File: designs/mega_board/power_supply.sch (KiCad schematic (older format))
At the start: 11 parts

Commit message: Add BOM definition to all resistors
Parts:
- R18, R60: Manufacturer (none) -> Panasonic Electronic Components; Manufacturer PN (none) -> ERJ-PA2F1003X; Supplier (none) -> DigiKey; Supplier PN (none) -> P17236DKR-ND
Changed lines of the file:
@@
 F 2 "LibreRouter_MegaBoard:R0402" V 2530 3650 50  0001 C CNN
 F 3 "~" H 2600 3650 50  0001 C CNN
+F 4 "Panasonic Electronic Components" H 2600 3650 50  0001 C CNN "Manufacturer"
+F 5 "ERJ-PA2F1003X" H 2600 3650 50  0001 C CNN "Manufacturer PN"
+F 6 "DigiKey" H 2600 3650 50  0001 C CNN "Supplier"
+F 7 "P17236DKR-ND" H 2600 3650 50  0001 C CNN "Supplier PN"
 	1    2600 3650
 	1    0    0    -1
@@
 F 2 "LibreRouter_MegaBoard:R0402" V 7480 3650 50  0001 C CNN
 F 3 "~" H 7550 3650 50  0001 C CNN
+F 4 "Panasonic Electronic Components" H 7550 3650 50  0001 C CNN "Manufacturer"
+F 5 "ERJ-PA2F1003X" H 7550 3650 50  0001 C CNN "Manufacturer PN"
+F 6 "DigiKey" H 7550 3650 50  0001 C CNN "Supplier"
+F 7 "P17236DKR-ND" H 7550 3650 50  0001 C CNN "Supplier PN"
 	1    7550 3650
 	1    0    0    -1

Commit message: Add some more BOM components definition
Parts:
- L1: Manufacturer (none) -> Littelfuse Inc.; Manufacturer PN (none) -> RUEF400-2; Supplier (none) -> DigiKey; Supplier PN (none) -> RUEF400-2HFCT-ND
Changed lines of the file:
@@
 F 2 "LibreRouter_MegaBoard:GR72-135" H 4150 900 50  0001 L CNN
 F 3 "~" H 4100 1100 50  0001 C CNN
+F 4 "Littelfuse Inc." H 4100 1100 50  0001 C CNN "Manufacturer"
+F 5 "RUEF400-2" H 4100 1100 50  0001 C CNN "Manufacturer PN"
+F 6 "DigiKey" H 4100 1100 50  0001 C CNN "Supplier"
+F 7 "RUEF400-2HFCT-ND" H 4100 1100 50  0001 C CNN "Supplier PN"
 	1    4100 1100
 	0    1    1    0

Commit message: Add some missing BOM details for components that are not in common suppliers
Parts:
- V1: Manufacturer (none) -> Bincheng Electronics; Manufacturer PN (none) -> BC301N-D
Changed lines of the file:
@@
 F 2 "LibreRouter_MegaBoard:BC301N-D" H 2900 1450 50  0001 C CNN
 F 3 "" H 2900 1450 50  0001 C CNN
+F 4 "Bincheng Electronics" H 2900 1450 50  0001 C CNN "Manufacturer"
+F 5 "BC301N-D" H 2900 1450 50  0001 C CNN "Manufacturer PN"
 	1    2900 1450
 	1    0    0    -1

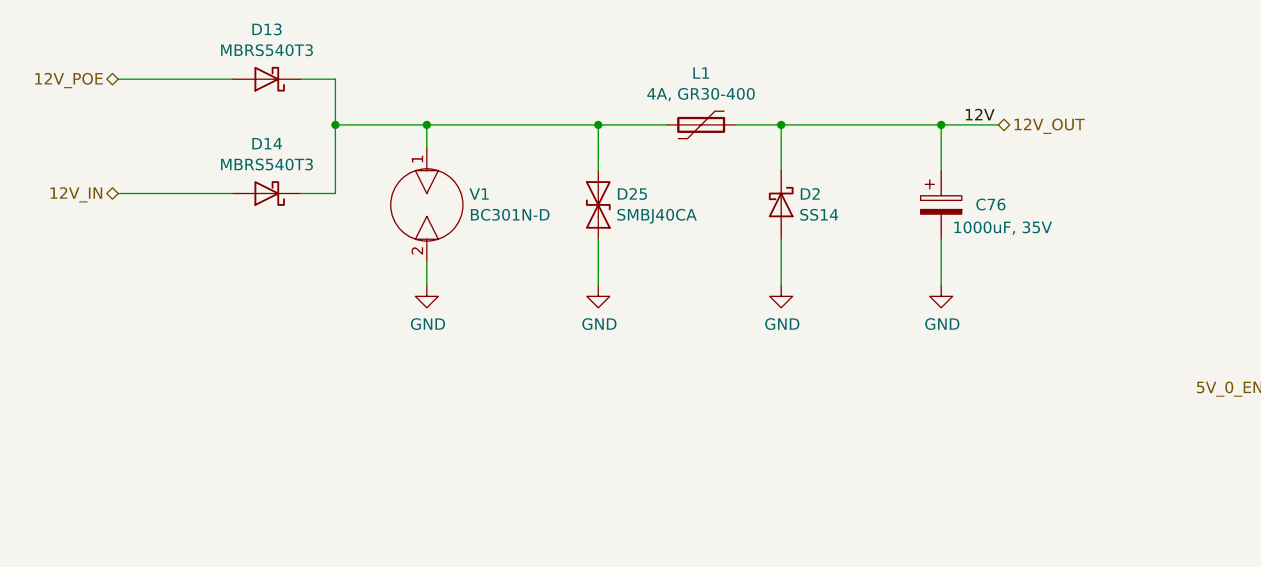
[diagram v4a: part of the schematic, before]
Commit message: Add poe input output dual circuit
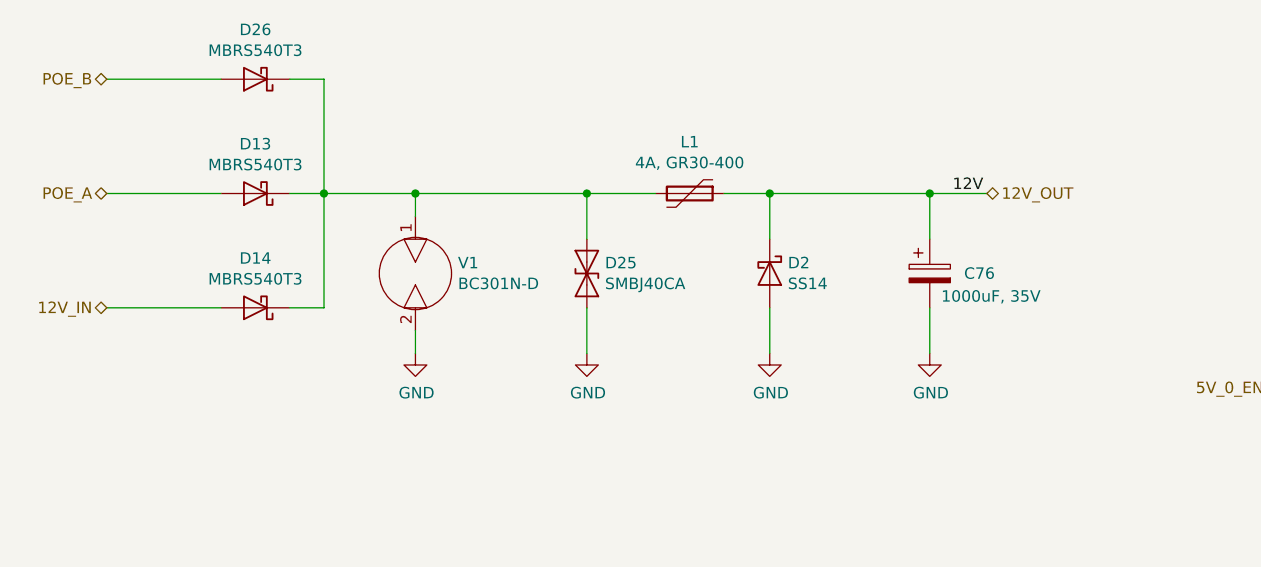
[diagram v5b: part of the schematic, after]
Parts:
- added D26: MBRS540T3, LibreRouter_MegaBoard:SMC, symbol Device:D_Schottky
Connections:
- net at D13.1 (K), D14.1 (K), D25.1 (A1)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: now also D26.1 (K)
- net 12V_POE renamed POE_A
- new net POE_B: D26.2 (A)
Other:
- moved on the sheet: C76, D13, D14, D2, D25, L1, V1

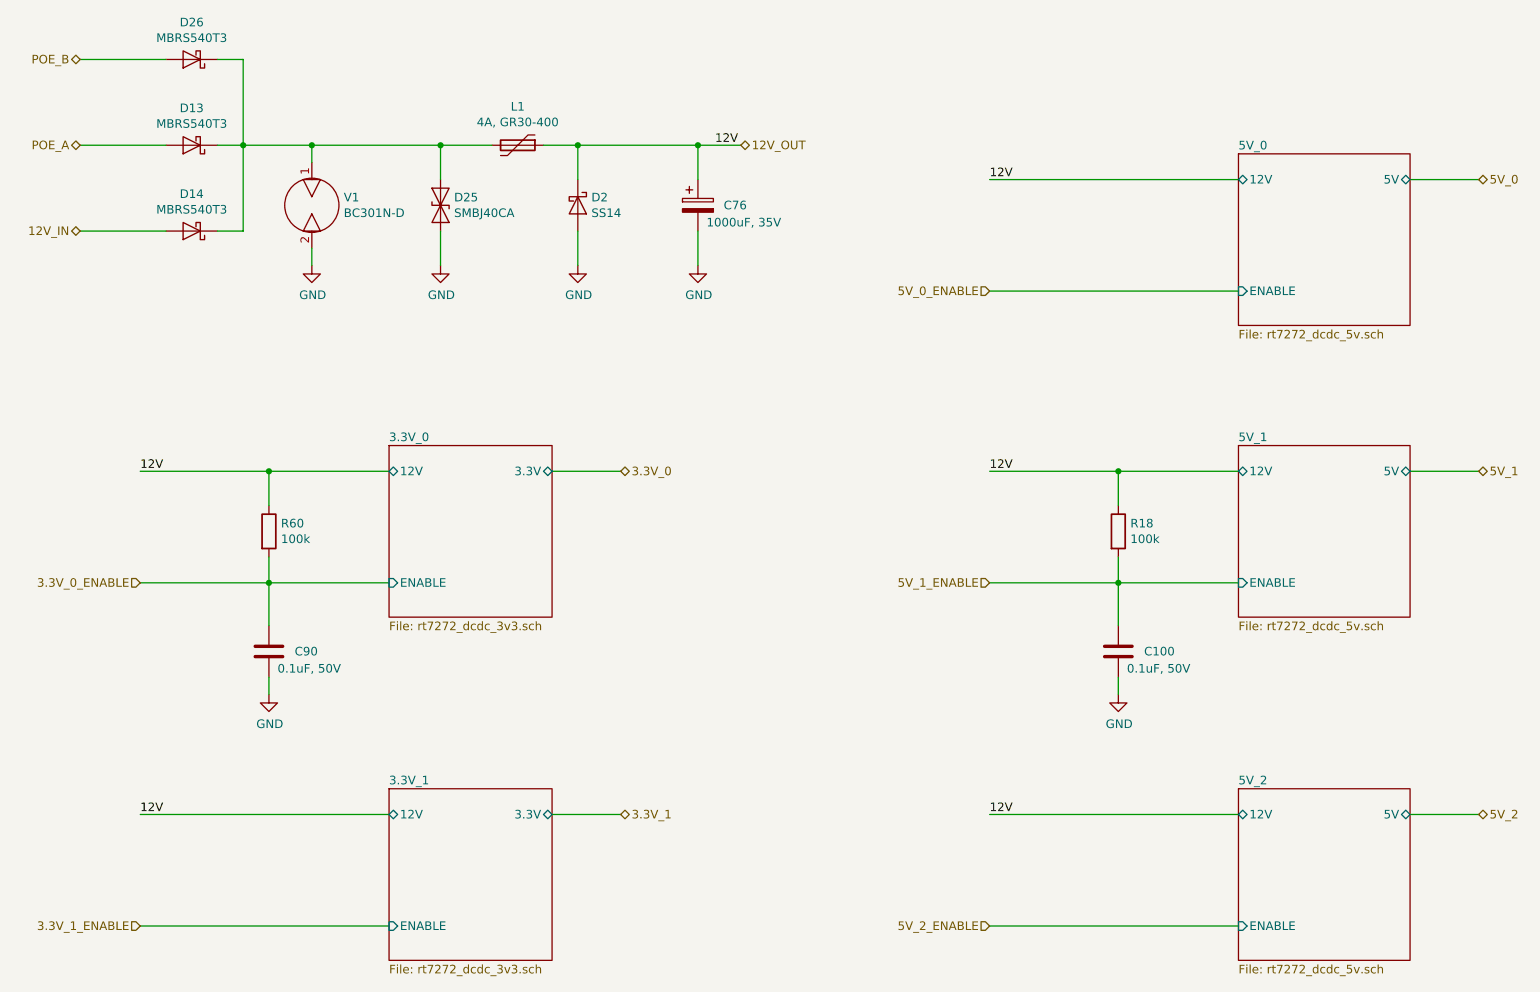
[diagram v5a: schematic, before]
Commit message: renamed net from +12V to VCC
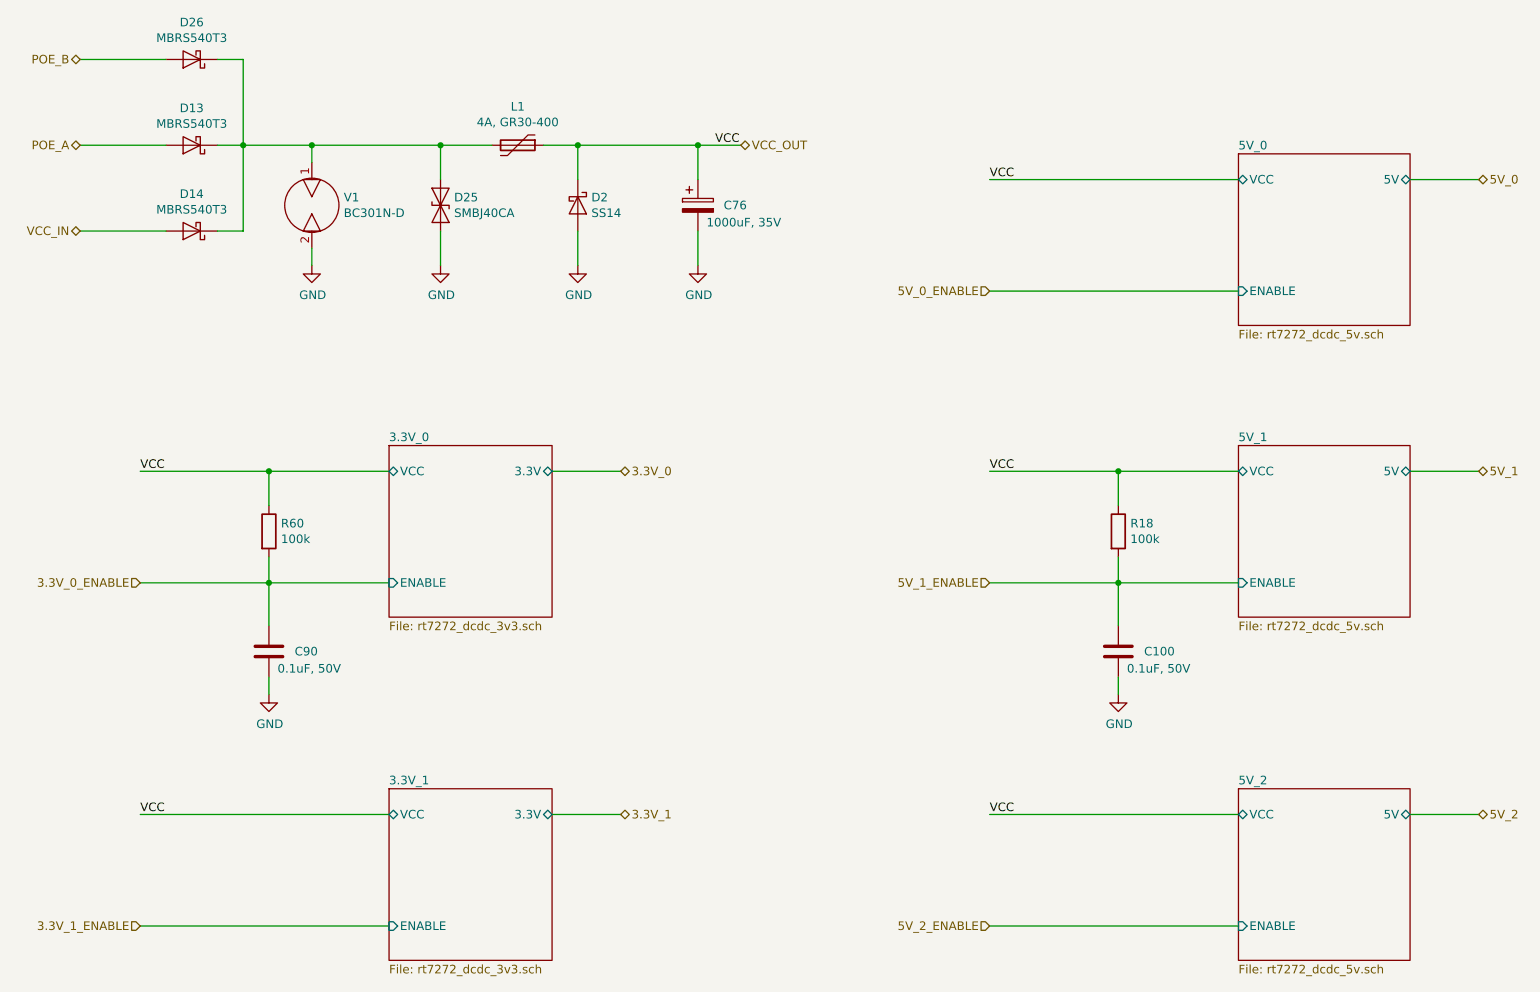
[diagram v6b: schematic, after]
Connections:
- net 12V_IN renamed VCC_IN
- net 12V_OUT renamed VCC_OUT
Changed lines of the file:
@@
 $EndDescr
 Text HLabel 5350 1400 2    50   BiDi ~ 0
-12V_OUT
+VCC_OUT
 Text HLabel 1500 1900 0    50   BiDi ~ 0
-12V_IN
+VCC_IN
 Text HLabel 9650 1600 2    50   BiDi ~ 0
 5V_0
@@
 POE_A
 $Sheet
-S 3300 5150 950  1000
-U 5D42CD47
-F0 "3.3V_1" 50
-F1 "rt7272_dcdc_3v3.sch" 50
-F2 "ENABLE" I L 3300 5950 50
-F3 "3.3V" B R 4250 5300 50
-F4 "12V" B L 3300 5300 50
-$EndSheet
-$Sheet
 S 3300 3150 950  1000
 U 5D42E225
@@
 F1 "rt7272_dcdc_3v3.sch" 50
 F2 "ENABLE" I L 3300 3950 50
-F3 "12V" B L 3300 3300 50
-F4 "3.3V" B R 4250 3300 50
+F3 "3.3V" B R 4250 3300 50
+F4 "VCC" B L 3300 3300 50
 $EndSheet
 $Comp
@@
 F1 "rt7272_dcdc_5v.sch" 50
 F2 "ENABLE" I L 8250 2250 50
-F3 "12V" B L 8250 1600 50
-F4 "5V" B R 9250 1600 50
+F3 "5V" B R 9250 1600 50
+F4 "VCC" B L 8250 1600 50
 $EndSheet
 Wire Wire Line
@@
 F1 "rt7272_dcdc_5v.sch" 50
 F2 "ENABLE" I L 8250 3950 50
-F3 "12V" B L 8250 3300 50
-F4 "5V" B R 9250 3300 50
+F3 "5V" B R 9250 3300 50
+F4 "VCC" B L 8250 3300 50
 $EndSheet
 $Comp
@@
 F1 "rt7272_dcdc_5v.sch" 50
 F2 "ENABLE" I L 8250 5950 50
-F3 "12V" B L 8250 5300 50
-F4 "5V" B R 9250 5300 50
+F3 "5V" B R 9250 5300 50
+F4 "VCC" B L 8250 5300 50
 $EndSheet
 Wire Wire Line
@@
 	3600 1400 2850 1400
 Text Label 5200 1400 0    50   ~ 0
-12V
+VCC
 Text Label 6800 1600 0    50   ~ 0
-12V
+VCC
 Text Label 6800 3300 0    50   ~ 0
-12V
+VCC
 Text Label 6800 5300 0    50   ~ 0
-12V
+VCC
 Text Label 1850 5300 0    50   ~ 0
-12V
+VCC
 Text Label 1850 3300 0    50   ~ 0
-12V
+VCC
 Text HLabel 1500 900  0    50   BiDi ~ 0
 POE_B
@@
 Wire Wire Line
 	2450 900  2450 1400
+$Sheet
+S 3300 5150 950  1000
+U 5D42CD47
+F0 "3.3V_1" 50
+F1 "rt7272_dcdc_3v3.sch" 50
+F2 "ENABLE" I L 3300 5950 50
+F3 "3.3V" B R 4250 5300 50
+F4 "VCC" B L 3300 5300 50
+$EndSheet
 $EndSCHEMATC
